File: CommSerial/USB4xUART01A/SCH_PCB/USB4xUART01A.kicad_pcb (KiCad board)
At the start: 2 copper layers, 70.6 x 40.1 mm, 94 parts, among them J1 JUMP_2x1, J10 JUMP_2x1, J11 JUMP_2x1, J12 JUMP_2x1, J13 JUMP_2x1, J14 JUMP_2x1, J15 JUMP_2x1, J16 JUMP_2x1, J17 JUMP_2x1, J18 JUMP_2x1, J19 JUMP_2x1, J2 JUMP_2x1, J20 JUMP_2x1, J21 JUMP_2x1, J22 JUMP_2x1, J23 JUMP_2x1, J24 JUMP_2x1, J25 JUMP_2x1, J26 JUMP_2x1, J27 JUMP_2x1, J28 JUMP_2x1, J29 JUMP_2x1, J3 JUMP_2x1, J30 JUMP_2x1, J31 JUMP_2x1, J32 JUMP_2x1, J33 JUMP_2x1, J34 JUMP_2x1, J35 JUMP_3X2, J36 JUMP_3X2, J4 JUMP_2x1, J5 JUMP_2x1, J6 JUMP_2x1, J7 JUMP_2x1, J8 JUMP_2x1, J9 JUMP_2x1, M1 HOLE, M2 HOLE, M3 HOLE, M4 HOLE, P1 USB_B, U1 93LC56BT-I/OT, U2 FT4232HL, U3 LM1117_3V3, U4 SN74HC595D, Y1 12MHz

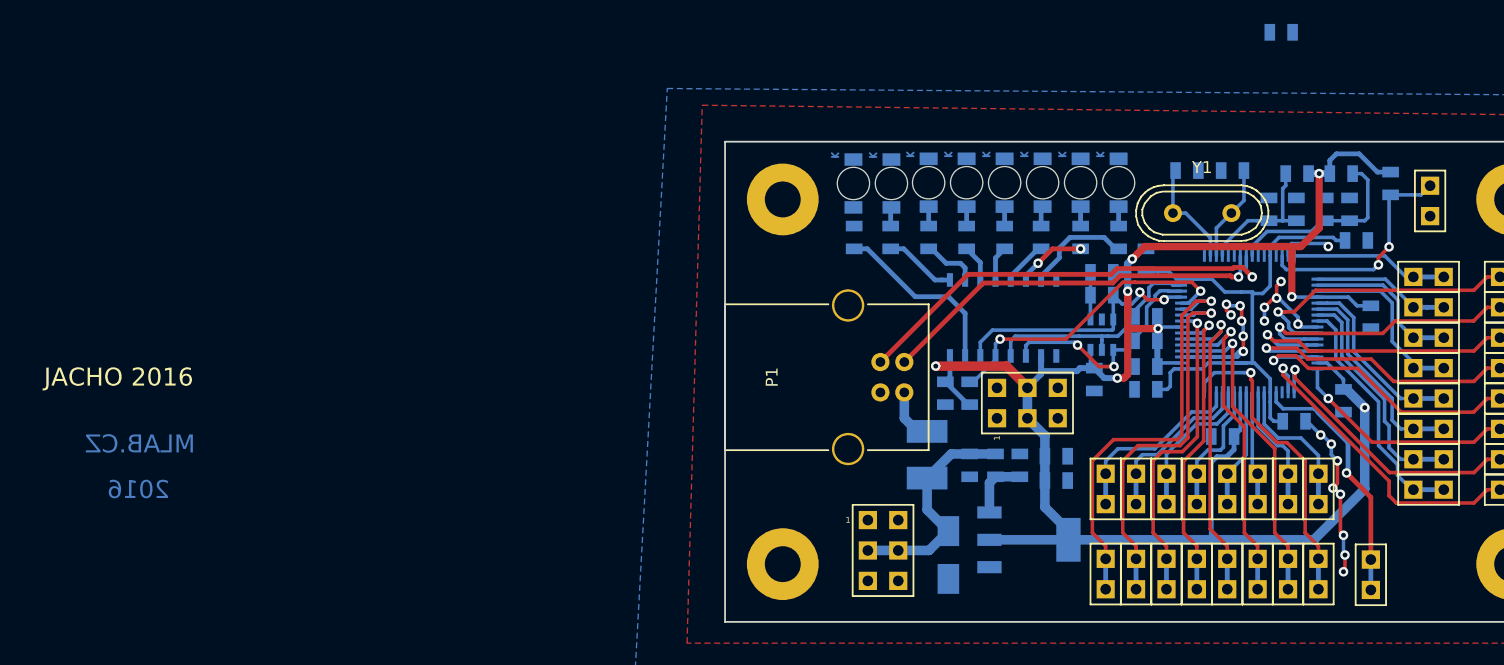
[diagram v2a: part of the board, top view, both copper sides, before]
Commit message: 
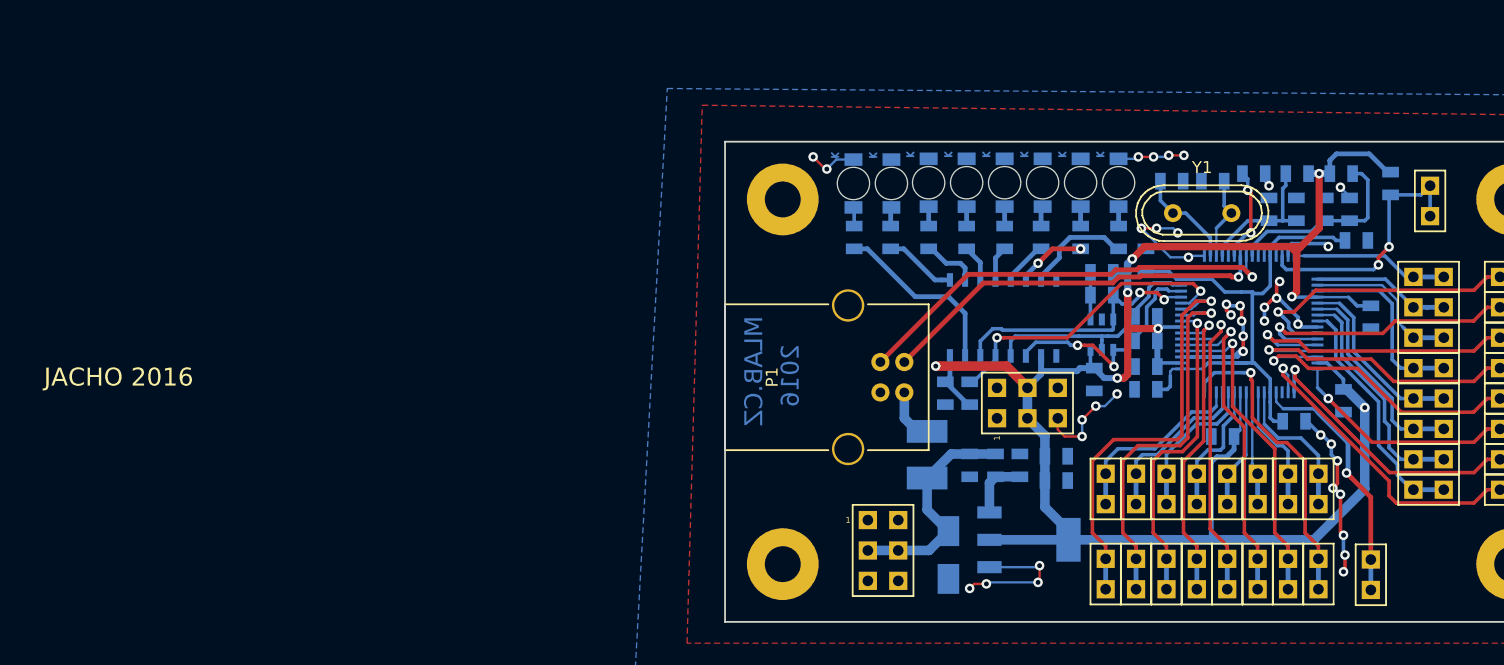
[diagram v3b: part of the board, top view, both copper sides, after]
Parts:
- moved R6 12.0 mm to (44.5, -37.7)
- moved C5 1.88 mm to (41.0, -37.1)
- moved C3 1.55 mm to (37.6, -37.1)
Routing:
- net GND: track 44.5 -> 86.0 mm, vias 20 -> 40
- net Net-(R6-Pad1): track 0.00 -> 7.88 mm, vias 0 -> 2
- net /RES: track 19.0 -> 21.6 mm
- net +3V3: track 185.3 -> 187.1 mm
- net Net-(D2-Pad2): track 0.00 -> 1.58 mm
- net Net-(C5-Pad1): track 8.08 -> 7.01 mm
- net /A_CTS: track 15.4 -> 16.0 mm
- net /B_CTS: track 28.0 -> 27.5 mm
- net Net-(C3-Pad1): track 9.13 -> 8.59 mm
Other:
- net class Default: trace_width 0.3 -> 0.2

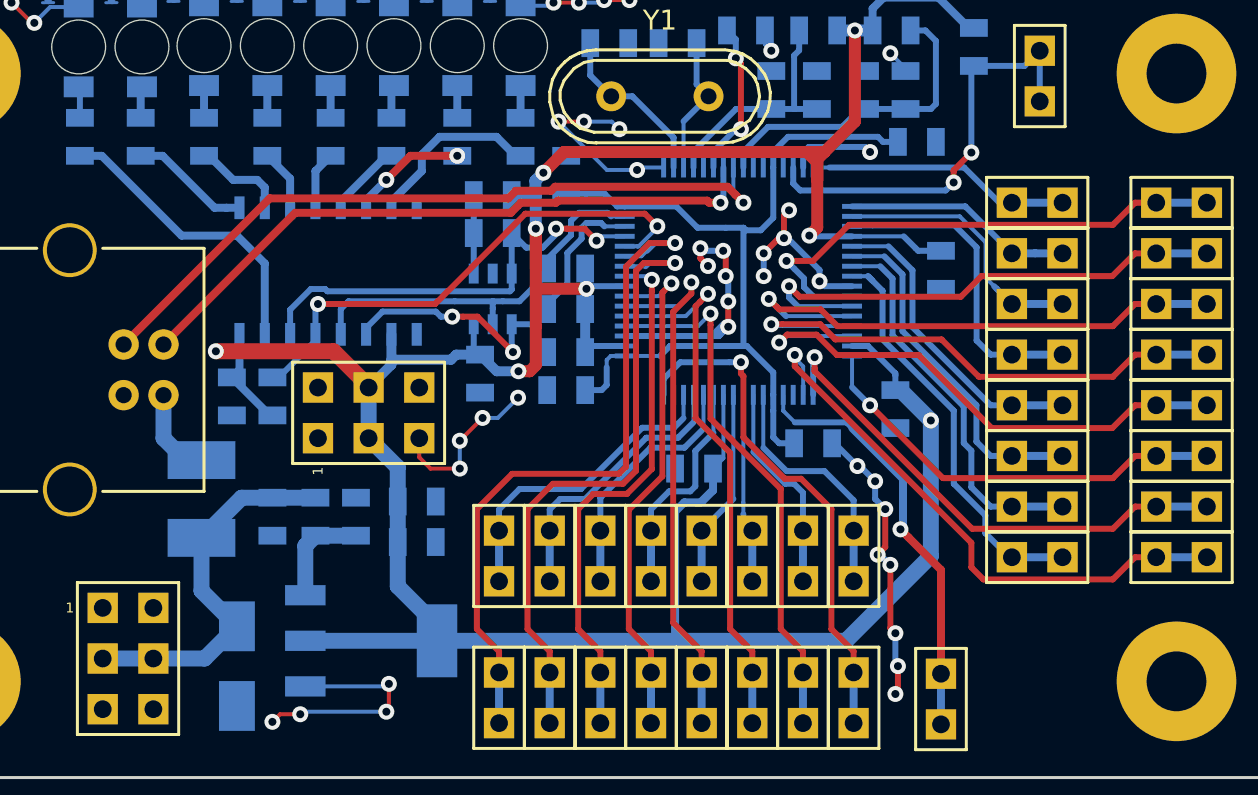
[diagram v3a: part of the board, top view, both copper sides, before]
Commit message: 
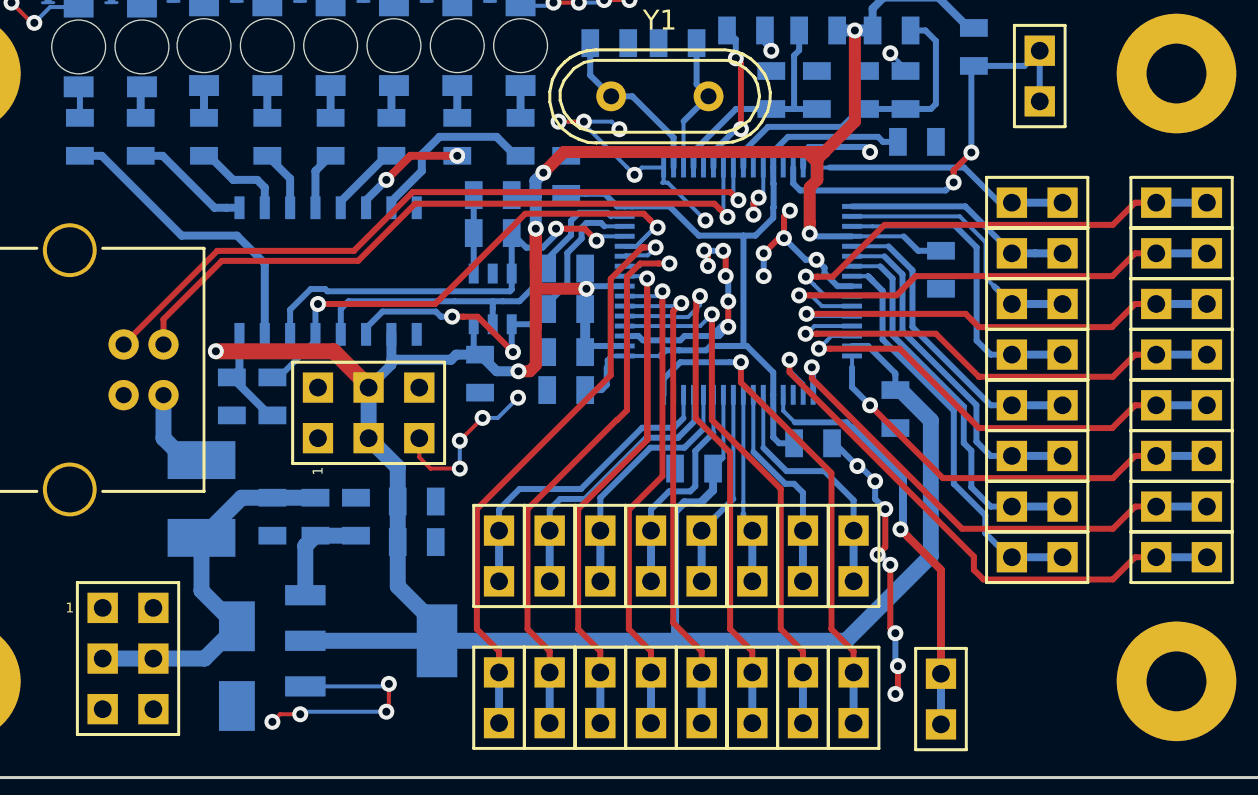
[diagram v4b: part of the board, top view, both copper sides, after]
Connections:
- net Net-(P1-Pad2) renamed /D-
- net Net-(P1-Pad3) renamed /D+
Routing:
- net /D_DSR: track 26.6 -> 33.4 mm
- net /D_RI: track 35.3 -> 30.2 mm
- net /B_RTS: track 27.5 -> 23.2 mm
- net /B_DTR: track 27.8 -> 23.5 mm
- net GND: track 86.0 -> 90.2 mm, vias 40 -> 43
- net /B_CTS: track 27.5 -> 24.0 mm
- net /#PWREN: track 26.1 -> 28.9 mm
- net /D_DCD: track 32.2 -> 29.6 mm
- net /D_CTS: track 27.2 -> 24.7 mm
- net /B_TXD: track 26.6 -> 24.4 mm
- net /D-: track 32.8 -> 34.8 mm
- net /B_RXD: track 26.0 -> 24.2 mm
- net /D_DTR: track 26.0 -> 24.8 mm
- net /D+: track 36.7 -> 35.9 mm
- net /B_DCD: track 26.0 -> 25.4 mm
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
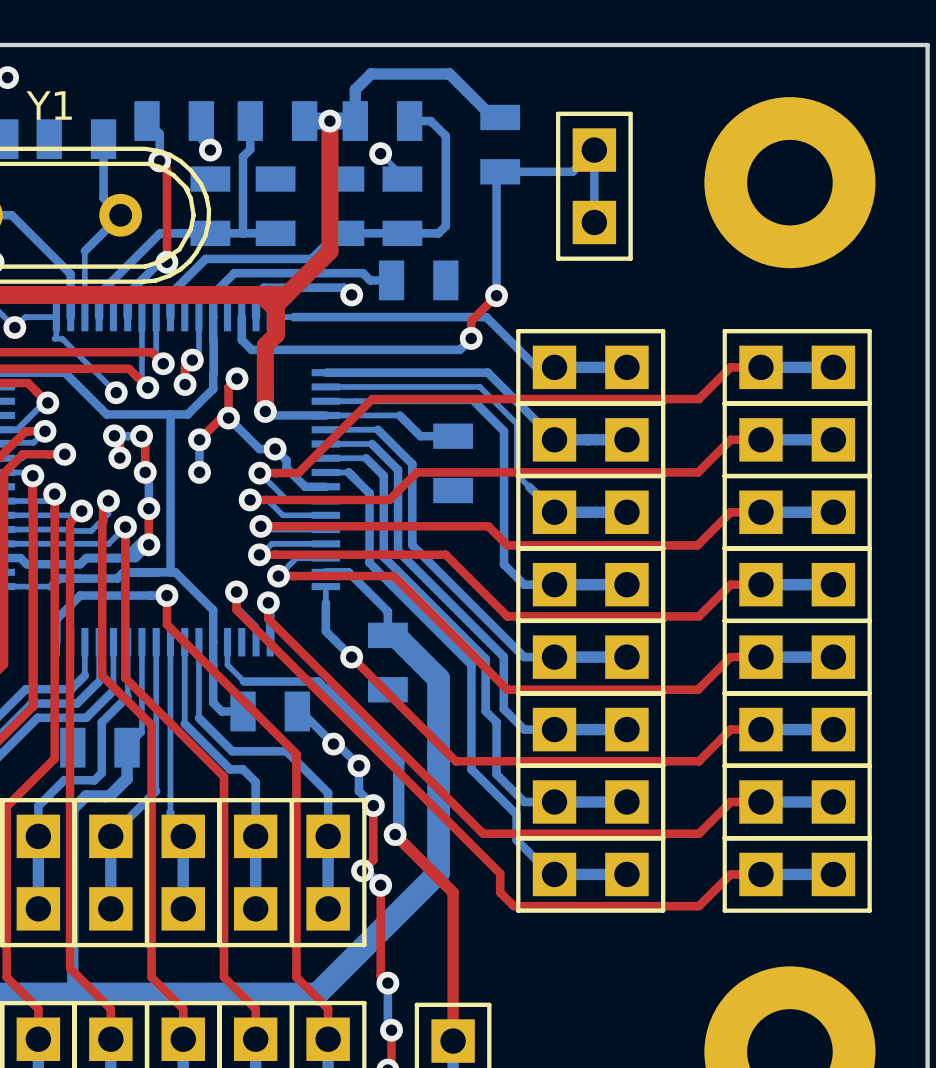
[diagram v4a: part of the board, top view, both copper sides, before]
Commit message: urava layoutu u IO.
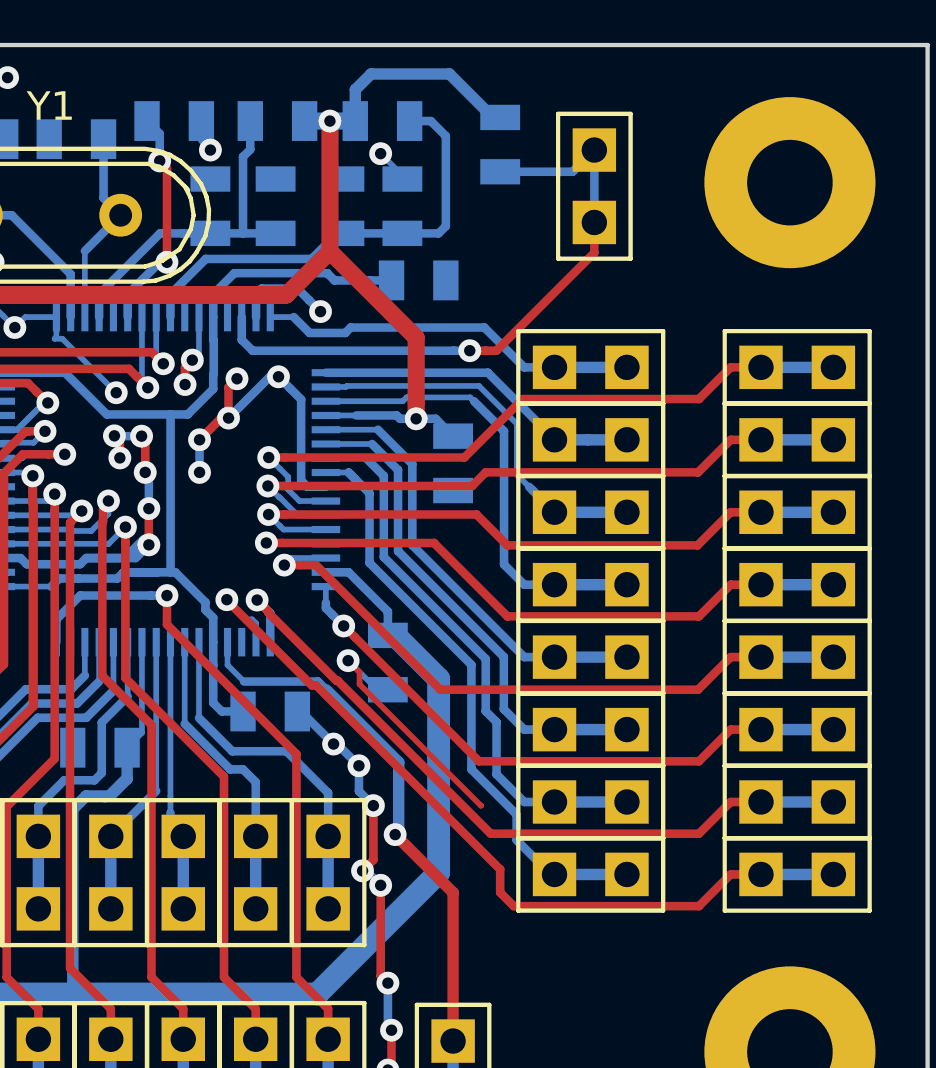
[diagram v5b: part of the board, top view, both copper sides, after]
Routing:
- net GND: track 90.2 -> 101.0 mm, vias 43 -> 44
- net /B_RXD: track 24.2 -> 23.0 mm
- net +3V3: track 187.0 -> 186.0 mm
- net /RES: track 21.6 -> 22.1 mm, vias 2 -> 1

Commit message: zmena
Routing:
- net /D_DSR: track 33.4 -> 25.4 mm
- net GND: track 101.0 -> 102.0 mm
- net /B_RI: track 28.7 -> 28.1 mm

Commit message: zmena
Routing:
- net GND: track 102.0 -> 87.4 mm, vias 44 -> 38
- net (no net): track 0.00 -> 5.86 mm, vias 0 -> 4
- net /#PWREN: track 28.9 -> 26.1 mm
- net /D_RTS: track 27.2 -> 25.5 mm
- net /D_RXD: track 27.0 -> 26.3 mm

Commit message: zmena
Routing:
- net GND: track 87.4 -> 94.3 mm, vias 38 -> 43
- net (no net): track 5.86 -> 0.00 mm, vias 4 -> 0
- net +3V3: track 186.0 -> 181.9 mm
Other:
- board text added: "#CTS"
- board text added: "#DCD"
- board text added: "#DSR"
- board text added: "#DTR"
- board text added: "#RES"
- board text added: "#RI"
- board text added: "#RTS"
- board text added: "#SUS"
- board text added: "+3V3"
- board text added: "+5V"
- board text added: "A"
- board text added: "B"
- board text added: "C"
- board text added: "D"
- board text added: "E"
- board text added: "F"
- board text added: "G"
- board text added: "H"
- board text added: "MLAB.CZ USB4xUART01A"
- board text added: "RXD"
- board text added: "TXD"
